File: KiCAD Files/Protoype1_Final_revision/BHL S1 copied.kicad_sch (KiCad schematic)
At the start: 94 parts, among them IC1 NUP2105LT1G, IC2 NUP2105LT1G, IC4 FD6288Q, J1 39-30-1042, J2 Conn_01x03_Pin, J3 Conn_01x03_Pin, J4 39-30-1042, Q1 CSD19502Q5B, Q2 CSD19502Q5B, Q3 CSD19502Q5B, Q4 CSD19502Q5B, Q5 CSD19502Q5B, Q7 CSD19502Q5B, U1 ME6211C30M5, U2 SPX3819M5-L-5-0, U3 Solder Pad, U5 STM32G431CBU6, Y1 8MHz

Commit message: Fixed all Errors in Schematic and Started routing PCB traces
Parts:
- removed R1: 0, Resistor_SMD:R_0402_1005Metric_Pad0.72x0.64mm_HandSolder, symbol Device:R
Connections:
- net DCBUS: now also J4.4
- net GND: now also J2.1 (Pin_1); no longer J2.2 (Pin_2)
- net SWCLK: now also J2.2 (Pin_2); no longer J2.1 (Pin_1)
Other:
- moved on the sheet: AS5600, C11, C12, C13, C14, C15, C16, C17, C33, D1, D2, D3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

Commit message: worked on PCB routing
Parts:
- R38: footprint Resistor_SMD:R_0603_1608Metric_Pad0.98x0.95mm_HandSolder -> Resistor_SMD:R_0402_1005Metric_Pad0.72x0.64mm_HandSolder
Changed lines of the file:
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@@
 			)
 		)
-		(property "Footprint" "Resistor_SMD:R_0603_1608Metric_Pad0.98x0.95mm_HandSolder"
+		(property "Footprint" "Resistor_SMD:R_0402_1005Metric_Pad0.72x0.64mm_HandSolder"
 			(at 126.492 113.03 90)
 			(effects

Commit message: Routed half the gate driver
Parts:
- C19, C20, C21: footprint Capacitor_SMD:C_0603_1608Metric_Pad1.08x0.95mm_HandSolder -> Capacitor_SMD:C_0402_1005Metric_Pad0.74x0.62mm_HandSolder
- C5: footprint Capacitor_SMD:C_0805_2012Metric_Pad1.18x1.45mm_HandSolder -> Capacitor_SMD:C_0603_1608Metric_Pad1.08x0.95mm_HandSolder
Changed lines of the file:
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@@
 			)
 		)
-		(property "Footprint" "Capacitor_SMD:C_0603_1608Metric_Pad1.08x0.95mm_HandSolder"
+		(property "Footprint" "Capacitor_SMD:C_0402_1005Metric_Pad0.74x0.62mm_HandSolder"
 			(at 373.0752 44.45 0)
 			(effects
@@
 			)
 		)
-		(property "Footprint" "Capacitor_SMD:C_0603_1608Metric_Pad1.08x0.95mm_HandSolder"
+		(property "Footprint" "Capacitor_SMD:C_0402_1005Metric_Pad0.74x0.62mm_HandSolder"
 			(at 322.2752 44.45 0)
 			(effects
@@
 			)
 		)
-		(property "Footprint" "Capacitor_SMD:C_0603_1608Metric_Pad1.08x0.95mm_HandSolder"
+		(property "Footprint" "Capacitor_SMD:C_0402_1005Metric_Pad0.74x0.62mm_HandSolder"
 			(at 266.3952 44.45 0)
 			(effects
@@
 			)
 		)
-		(property "Footprint" "Capacitor_SMD:C_0805_2012Metric_Pad1.18x1.45mm_HandSolder"
+		(property "Footprint" "Capacitor_SMD:C_0603_1608Metric_Pad1.08x0.95mm_HandSolder"
 			(at 389.5852 125.73 0)
 			(effects

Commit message: Finished Routing the Gate Driver!
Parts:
- R20, R23, R26: footprint Resistor_SMD:R_0603_1608Metric_Pad0.98x0.95mm_HandSolder -> Resistor_SMD:R_1206_3216Metric_Pad1.30x1.75mm_HandSolder
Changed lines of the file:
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@@
 			)
 		)
-		(property "Footprint" "Resistor_SMD:R_0603_1608Metric_Pad0.98x0.95mm_HandSolder"
+		(property "Footprint" "Resistor_SMD:R_1206_3216Metric_Pad1.30x1.75mm_HandSolder"
 			(at 272.542 78.74 90)
 			(effects
@@
 			)
 		)
-		(property "Footprint" "Resistor_SMD:R_0603_1608Metric_Pad0.98x0.95mm_HandSolder"
+		(property "Footprint" "Resistor_SMD:R_1206_3216Metric_Pad1.30x1.75mm_HandSolder"
 			(at 349.25 102.362 90)
 			(effects
@@
 			)
 		)
-		(property "Footprint" "Resistor_SMD:R_0603_1608Metric_Pad0.98x0.95mm_HandSolder"
+		(property "Footprint" "Resistor_SMD:R_1206_3216Metric_Pad1.30x1.75mm_HandSolder"
 			(at 334.518 91.44 90)
 			(effects

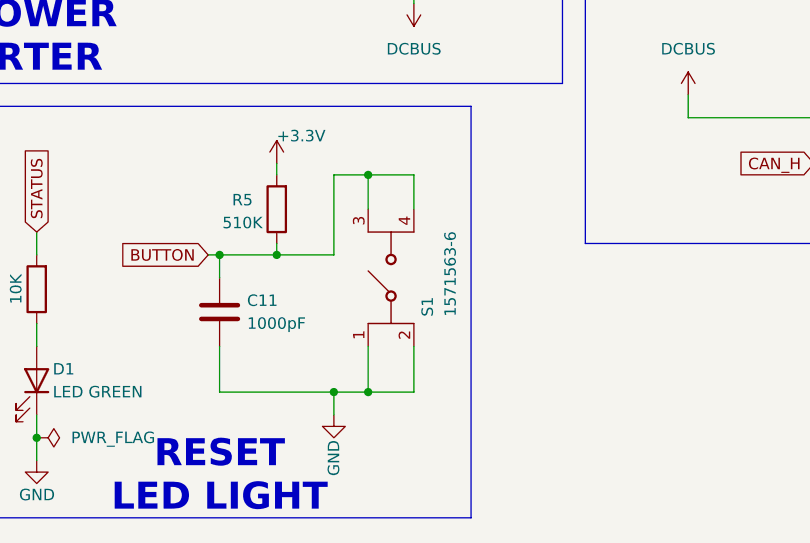
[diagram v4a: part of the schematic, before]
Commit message: Can Bus Routed In PCB
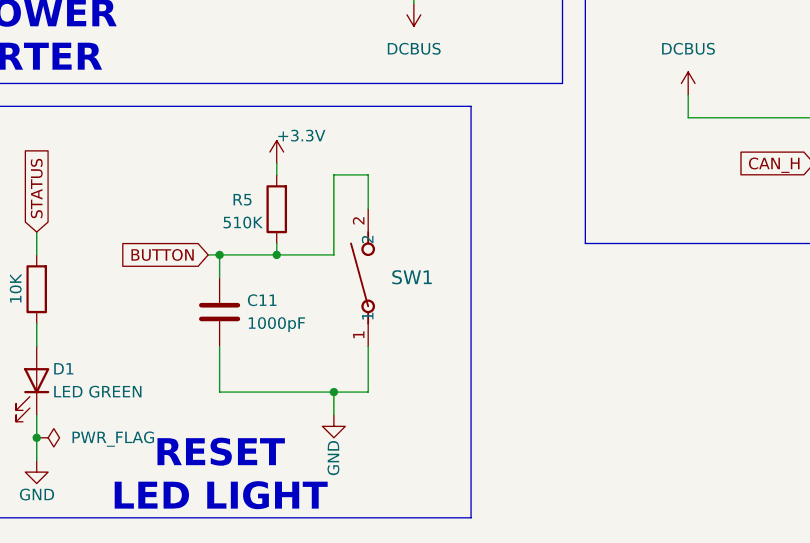
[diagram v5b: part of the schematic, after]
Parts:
- removed S1: 1571563-6, Footprint for BHL S1:Push Button 6x6mm, symbol BHLS1_PUSHBUT:1571563-6
- added SW1: PTS636 SM50J SMTR LFS, Footprint for BHL S1:SW_PTS636_CNK, symbol BHL_S1_CUSTOMED:Tactile_Switch
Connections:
- net BUTTON: now also SW1.2
- net GND: now also SW1.1
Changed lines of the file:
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@@
 	)
 	(junction
-		(at 285.75 243.84)
-		(diameter 0)
-		(color 0 0 0 0)
-	)
-	(junction
 		(at 165.1 196.85)
 		(diameter 0)
@@
 	)
 	(junction
-		(at 285.75 267.97)
-		(diameter 0)
-		(color 0 0 0 0)
-	)
-	(junction
 		(at 128.27 189.23)
 		(diameter 0)
@@
 	(wire
 		(pts
-			(xy 285.75 267.97) (xy 290.83 267.97)
-		)
-		(stroke
-			(width 0)
-			(type default)
-		)
-	)
-	(wire
-		(pts
 			(xy 123.19 96.52) (xy 125.73 96.52)
 		)
@@
 	(wire
 		(pts
-			(xy 285.75 243.84) (xy 290.83 243.84)
-		)
-		(stroke
-			(width 0)
-			(type default)
-		)
-	)
-	(wire
-		(pts
 			(xy 379.73 81.28) (xy 379.73 86.36)
 		)
@@
 	(wire
 		(pts
-			(xy 290.83 243.84) (xy 290.83 247.65)
-		)
-		(stroke
-			(width 0)
-			(type default)
-		)
-	)
-	(wire
-		(pts
 			(xy 248.92 35.56) (xy 248.92 43.18)
 		)
@@
 	(wire
 		(pts
-			(xy 290.83 267.97) (xy 290.83 262.89)
-		)
-		(stroke
-			(width 0)
-			(type default)
-		)
-	)
-	(wire
-		(pts
 			(xy 255.27 72.39) (xy 274.32 72.39)
 		)
@@
 	)
 	(symbol
+		(lib_id "BHL_S1_CUSTOMED:Tactile_Switch")
+		(at 285.75 262.89 90)
+		(unit 1)
+		(exclude_from_sim no)
+		(in_bom yes)
+		(on_board yes)
+		(dnp no)
+		(fields_autoplaced yes)
+		(property "Reference" "SW1"
+			(at 288.29 255.2699 90)
+			(effects
+				(font
+					(size 1.524 1.524)
+				)
+				(justify right)
+			)
+		)
+		(property "Value" "PTS636 SM50J SMTR LFS"
+			(at 288.544 260.604 0)
+			(effects
+				(font
+					(size 1.524 1.524)
+				)
+				(hide yes)
+			)
+		)
+		(property "Footprint" "Footprint for BHL S1:SW_PTS636_CNK"
+			(at 285.75 262.89 0)
+			(effects
+				(font
+					(size 1.27 1.27)
+					(italic yes)
+				)
+				(hide yes)
+			)
+		)
+		(property "Datasheet" "PTS636 SM50J SMTR LFS"
+			(at 285.75 262.89 0)
+			(effects
+				(font
+					(size 1.27 1.27)
+					(italic yes)
+				)
+				(hide yes)
+			)
+		)
+		(property "Description" ""
+			(at 285.75 262.89 0)
+			(effects
+				(font
+					(size 1.27 1.27)
+				)
+				(hide yes)
+			)
+		)
+		(pin "1"
+		)
+		(pin "2"
+		)
+		(instances
+			(project ""
+				(path "/0363b2da-c10c-4051-b2e0-f0863b63e8b4"
+					(reference "SW1")
+					(unit 1)
+				)
+			)
+		)
+	)
+	(symbol
 		(lib_id "Device:R")
 		(at 77.47 201.93 180)
@@
 					(unit 1)
 				)
-			)
-		)
-	)
-	(symbol
-		(lib_id "BHLS1_PUSHBUT:1571563-6")
-		(at 285.75 262.89 90)
-		(unit 1)
-		(exclude_from_sim no)
-		(in_bom yes)
-		(on_board yes)
-		(dnp no)
-		(property "Reference" "S1"
-			(at 292.354 259.588 0)
-			(effects
-				(font
-					(size 1.27 1.27)
-				)
-				(justify left)
-			)
-		)
-		(property "Value" "1571563-6"
-			(at 294.894 259.588 0)
-			(effects
-				(font
-					(size 1.27 1.27)
-				)
-				(justify left)
-			)
-		)
-		(property "Footprint" "Footprint for BHL S1:Push Button 6x6mm"
-			(at 284.48 250.19 0)
-			(effects
-				(font
-					(size 1.27 1.27)
-				)
-				(justify left)
-				(hide yes)
-			)
-		)
-		(property "Datasheet" "https://www.te.com/commerce/DocumentDelivery/DDEController?Action=srchrtrv&DocNm=1977223&DocType=Customer%20Drawing&DocLang=English&DocFormat=pdf&PartCntxt=2-1977223-2"
-			(at 287.02 250.19 0)
-			(effects
-				(font
-					(size 1.27 1.27)
-				)
-				(justify left)
-				(hide yes)
-			)
-		)
-		(property "Description" ""
-			(at 285.75 262.89 0)
-			(effects
-				(font
-					(size 1.27 1.27)
-				)
-				(hide yes)
-			)
-		)
-		(property "Description_1" "50 mA Tactile Switch, Round Actuator, Off (On), Phosphor Bronze, Silver Contact Plating, 24 VDC, ALCOSWITCH FSMJSMA"
-			(at 289.56 250.19 0)
-			(effects
-				(font
-					(size 1.27 1.27)
-				)
-				(justify left)
-				(hide yes)
-			)
-		)
-		(property "Height" "13.25"
-			(at 292.1 250.19 0)
-			(effects
-				(font
-					(size 1.27 1.27)
-				)
-				(justify left)
-				(hide yes)
-			)
-		)
-		(property "Mouser Part Number" "506-1571563-6"
-			(at 294.64 250.19 0)
-			(effects
-				(font
-					(size 1.27 1.27)
-				)
-				(justify left)
-				(hide yes)
-			)
-		)
-		(property "Mouser Price/Stock" "https://www.mouser.co.uk/ProductDetail/TE-Connectivity-PB/1571563-6?qs=kSbAZawwBnzmioGrnhYP0w%3D%3D"
-			(at 297.18 250.19 0)
-			(effects
-				(font
-					(size 1.27 1.27)
-				)
-				(justify left)
-				(hide yes)
-			)
-		)
-		(property "Manufacturer_Name" "TE Connectivity"
-			(at 299.72 250.19 0)
-			(effects
-				(font
-					(size 1.27 1.27)
-				)
-				(justify left)
-				(hide yes)
-			)
-		)
-		(property "Manufacturer_Part_Number" "1571563-6"
-			(at 302.26 250.19 0)
-			(effects
-				(font
-					(size 1.27 1.27)
-				)
-				(justify left)
-				(hide yes)
-			)
-		)
-		(pin "1"
-		)
-		(pin "2"
-		)
-		(pin "4"
-		)
-		(pin "3"
-		)
-		(instances
-			(project ""
-				(path "/0363b2da-c10c-4051-b2e0-f0863b63e8b4"
-					(reference "S1")
-					(unit 1)
-				)

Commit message: Finished the Board!!
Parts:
- C2: footprint Capacitor_SMD:C_0805_2012Metric_Pad1.18x1.45mm_HandSolder -> Capacitor_SMD:C_0402_1005Metric_Pad0.74x0.62mm_HandSolder
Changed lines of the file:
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@@
 			)
 		)
-		(property "Footprint" "Capacitor_SMD:C_0805_2012Metric_Pad1.18x1.45mm_HandSolder"
+		(property "Footprint" "Capacitor_SMD:C_0402_1005Metric_Pad0.74x0.62mm_HandSolder"
 			(at 167.3352 168.91 0)
 			(effects

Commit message: Finished Revision
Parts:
- R20, R23, R26: footprint Resistor_SMD:R_1206_3216Metric_Pad1.30x1.75mm_HandSolder -> Resistor_SMD:R_2512_6332Metric_Pad1.40x3.35mm_HandSolder
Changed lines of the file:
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@@
 			)
 		)
-		(property "Footprint" "Resistor_SMD:R_1206_3216Metric_Pad1.30x1.75mm_HandSolder"
+		(property "Footprint" "Resistor_SMD:R_2512_6332Metric_Pad1.40x3.35mm_HandSolder"
 			(at 272.542 78.74 90)
 			(effects
@@
 			)
 		)
-		(property "Footprint" "Resistor_SMD:R_1206_3216Metric_Pad1.30x1.75mm_HandSolder"
+		(property "Footprint" "Resistor_SMD:R_2512_6332Metric_Pad1.40x3.35mm_HandSolder"
 			(at 349.25 102.362 90)
 			(effects
@@
 			)
 		)
-		(property "Footprint" "Resistor_SMD:R_1206_3216Metric_Pad1.30x1.75mm_HandSolder"
+		(property "Footprint" "Resistor_SMD:R_2512_6332Metric_Pad1.40x3.35mm_HandSolder"
 			(at 334.518 91.44 90)
 			(effects

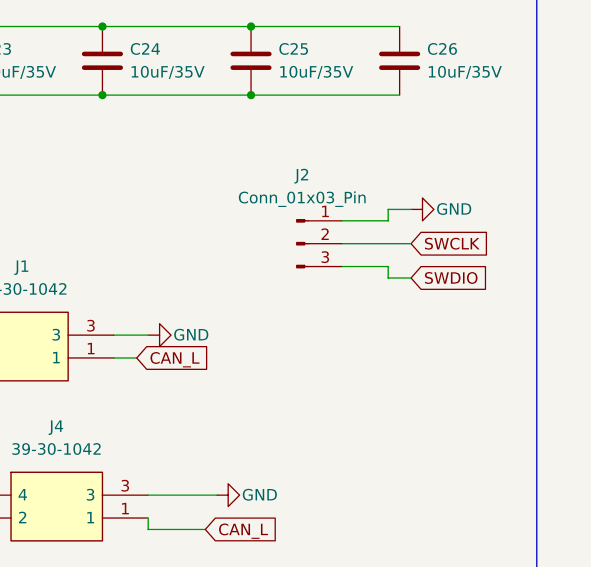
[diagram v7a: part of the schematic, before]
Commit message: Made some fixes to the PCB
Fixed Diode, trace sizes, and placements
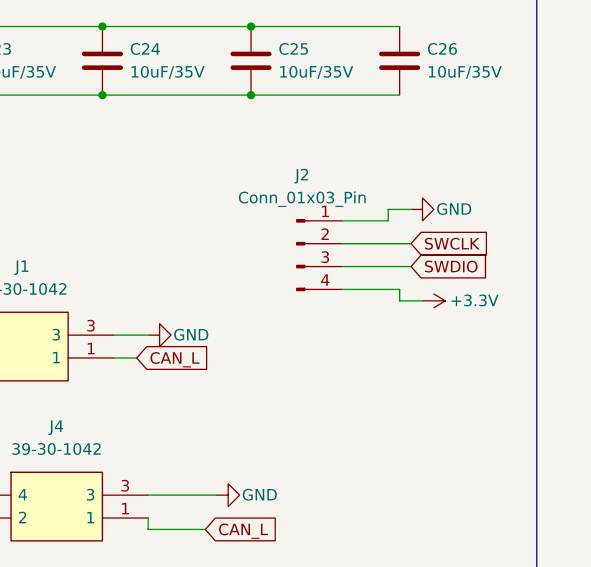
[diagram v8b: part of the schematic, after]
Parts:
- D2, D3: footprint Diode_SMD:D_SOD-523 -> Footprint for BHL S1:DIO_STPS1L40M
- J2: footprint Connector_PinHeader_2.54mm:PinHeader_1x03_P2.54mm_Vertical -> Connector_PinHeader_2.54mm:PinHeader_1x04_P2.54mm_Vertical; symbol Connector:Conn_01x03_Pin -> Connector:Conn_01x04_Pin
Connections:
- net +3.3V: now also J2.4 (Pin_4)
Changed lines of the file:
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@@
 	(wire
 		(pts
-			(xy 387.35 212.09) (xy 387.35 213.36)
-		)
-		(stroke
-			(width 0)
-			(type default)
-		)
-	)
-	(wire
-		(pts
 			(xy 388.62 139.7) (xy 392.43 139.7)
 		)
@@
 	(wire
 		(pts
+			(xy 388.62 215.9) (xy 391.16 215.9)
+		)
+		(stroke
+			(width 0)
+			(type default)
+		)
+	)
+	(wire
+		(pts
 			(xy 74.93 76.2) (xy 77.47 76.2)
 		)
@@
 	(wire
 		(pts
+			(xy 382.27 214.63) (xy 388.62 214.63)
+		)
+		(stroke
+			(width 0)
+			(type default)
+		)
+	)
+	(wire
+		(pts
 			(xy 166.37 160.02) (xy 173.99 160.02)
 		)
@@
 	(wire
 		(pts
-			(xy 387.35 213.36) (xy 389.89 213.36)
-		)
-		(stroke
-			(width 0)
-			(type default)
-		)
-	)
-	(wire
-		(pts
 			(xy 146.05 251.46) (xy 146.05 254)
 		)
@@
 	(wire
 		(pts
+			(xy 388.62 214.63) (xy 388.62 215.9)
+		)
+		(stroke
+			(width 0)
+			(type default)
+		)
+	)
+	(wire
+		(pts
 			(xy 331.47 50.8) (xy 331.47 55.88)
 		)
@@
 	(wire
 		(pts
-			(xy 382.27 212.09) (xy 387.35 212.09)
+			(xy 382.27 212.09) (xy 389.89 212.09)
 		)
 		(stroke
@@
 	(global_label "SWDIO"
 		(shape input)
-		(at 389.89 213.36 0)
+		(at 389.89 212.09 0)
 		(fields_autoplaced yes)
 		(effects
@@
 		)
 		(property "Intersheetrefs" "${INTERSHEET_REFS}"
-			(at 398.7414 213.36 0)
+			(at 398.7414 212.09 0)
 			(effects
 				(font
@@
 	)
 	(symbol
-		(lib_id "Connector:Conn_01x03_Pin")
+		(lib_id "Connector:Conn_01x04_Pin")
 		(at 377.19 209.55 0)
 		(unit 1)
@@
 			)
 		)
-		(property "Footprint" "Connector_PinHeader_2.54mm:PinHeader_1x03_P2.54mm_Vertical"
+		(property "Footprint" "Connector_PinHeader_2.54mm:PinHeader_1x04_P2.54mm_Vertical"
 			(at 377.19 209.55 0)
 			(effects
@@
 			)
 		)
-		(property "Description" "Generic connector, single row, 01x03, script generated"
+		(property "Description" "Generic connector, single row, 01x04, script generated"
 			(at 377.19 209.55 0)
 			(effects
@@
 		(pin "3"
 		)
+		(pin "4"
+		)
 		(instances
 			(project ""
@@
 			)
 		)
-		(property "Footprint" "Diode_SMD:D_SOD-523"
+		(property "Footprint" "Footprint for BHL S1:DIO_STPS1L40M"
 			(at 275.59 210.185 0)
 			(effects
@@
 			)
 		)
-		(property "Footprint" "Diode_SMD:D_SOD-523"
+		(property "Footprint" "Footprint for BHL S1:DIO_STPS1L40M"
 			(at 287.02 226.695 0)
 			(effects
@@
 					(unit 1)
 				)
+			)
+		)
+	)
+	(symbol
+		(lib_id "power:+3.3V")
+		(at 391.16 215.9 270)
+		(unit 1)
+		(exclude_from_sim no)
+		(in_bom yes)
+		(on_board yes)
+		(dnp no)
+		(property "Reference" "#PWR017"
+			(at 387.35 215.9 0)
+			(effects
+				(font
+					(size 1.27 1.27)
+				)
+				(hide yes)
+			)
+		)
+		(property "Value" "+3.3V"
+			(at 394.208 215.9 90)
+			(effects
+				(font
+					(size 1.27 1.27)
+				)
+				(justify left)
+			)
+		)
+		(property "Footprint" ""
+			(at 391.16 215.9 0)
+			(effects
+				(font
+					(size 1.27 1.27)
+				)
+				(hide yes)
+			)
+		)
+		(property "Datasheet" ""
+			(at 391.16 215.9 0)
+			(effects
+				(font
+					(size 1.27 1.27)
+				)
+				(hide yes)
+			)
+		)
+		(property "Description" "Power symbol creates a global label with name \"+3.3V\""
+			(at 391.16 215.9 0)
+			(effects
+				(font
+					(size 1.27 1.27)
+				)
+				(hide yes)
+			)
+		)
+		(pin "1"
+		)
+		(instances
+			(project "BHL S1 copied"
+				(path "/0363b2da-c10c-4051-b2e0-f0863b63e8b4"
+					(reference "#PWR017")
+					(unit 1)
+				)
